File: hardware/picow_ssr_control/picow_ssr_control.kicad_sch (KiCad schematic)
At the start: 29 parts, among them Q1 IRF4905PBF, Q2 DMG2301L, U1 RaspberryPi-PicoW, U2 ULN2803A

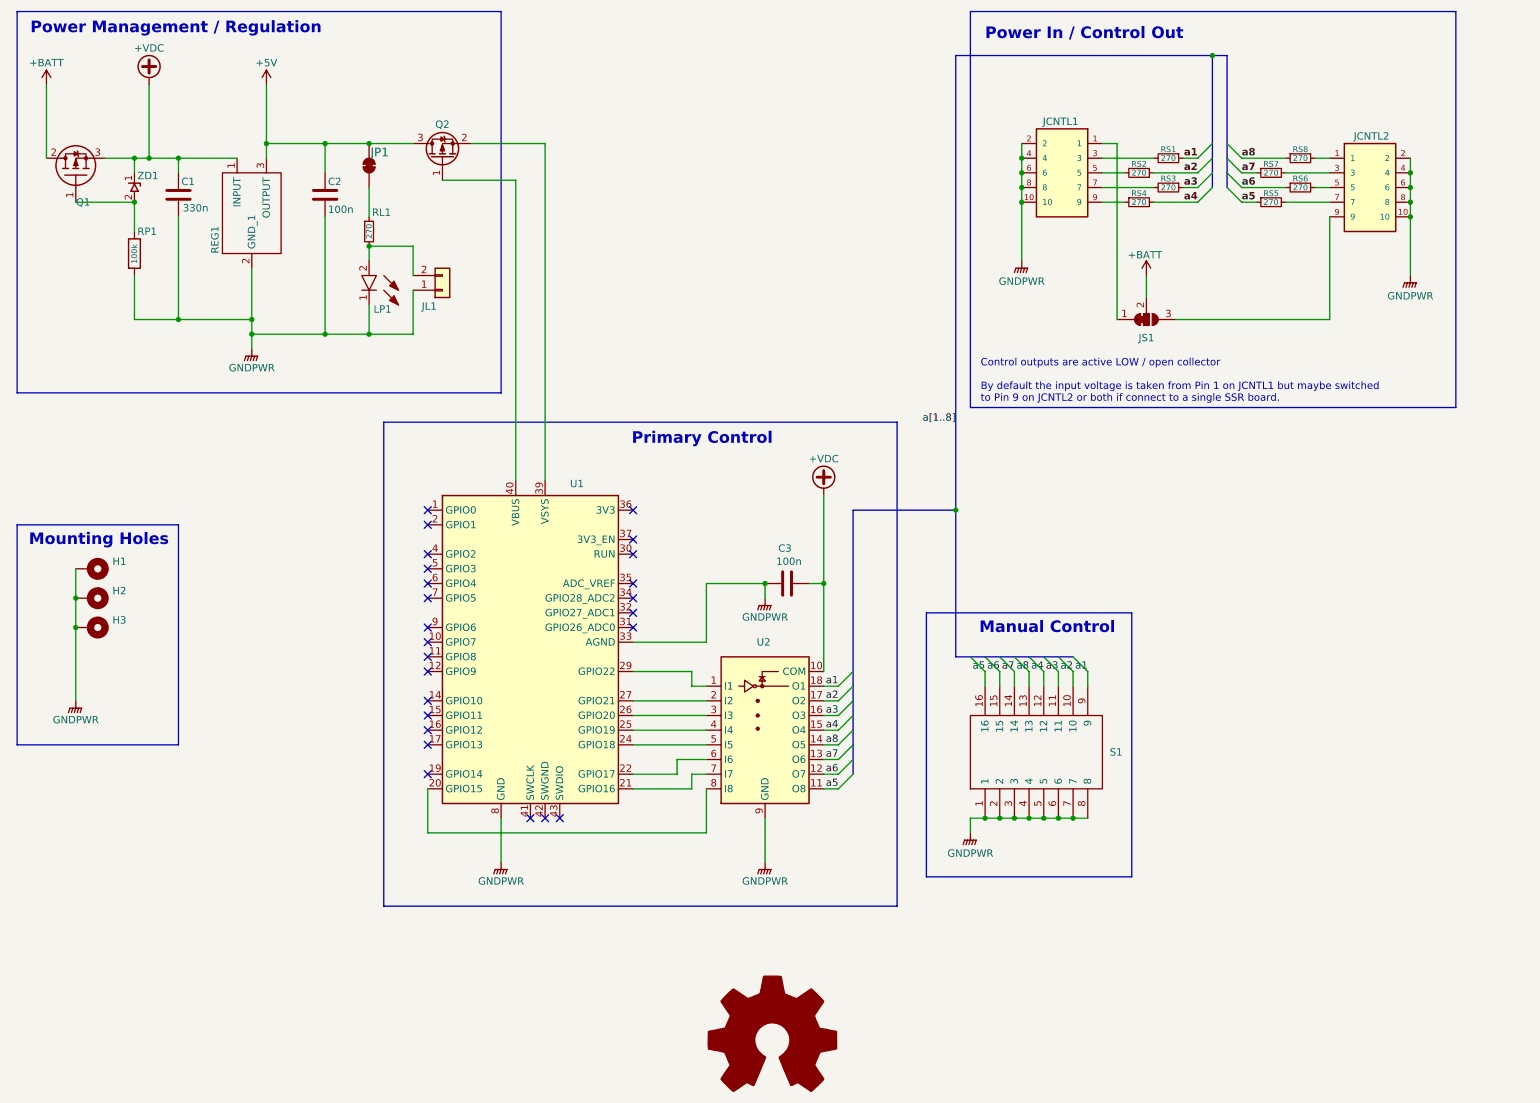
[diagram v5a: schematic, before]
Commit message: Replaced un-obtainable ULN2803 with SMD FETs and updated control connectors
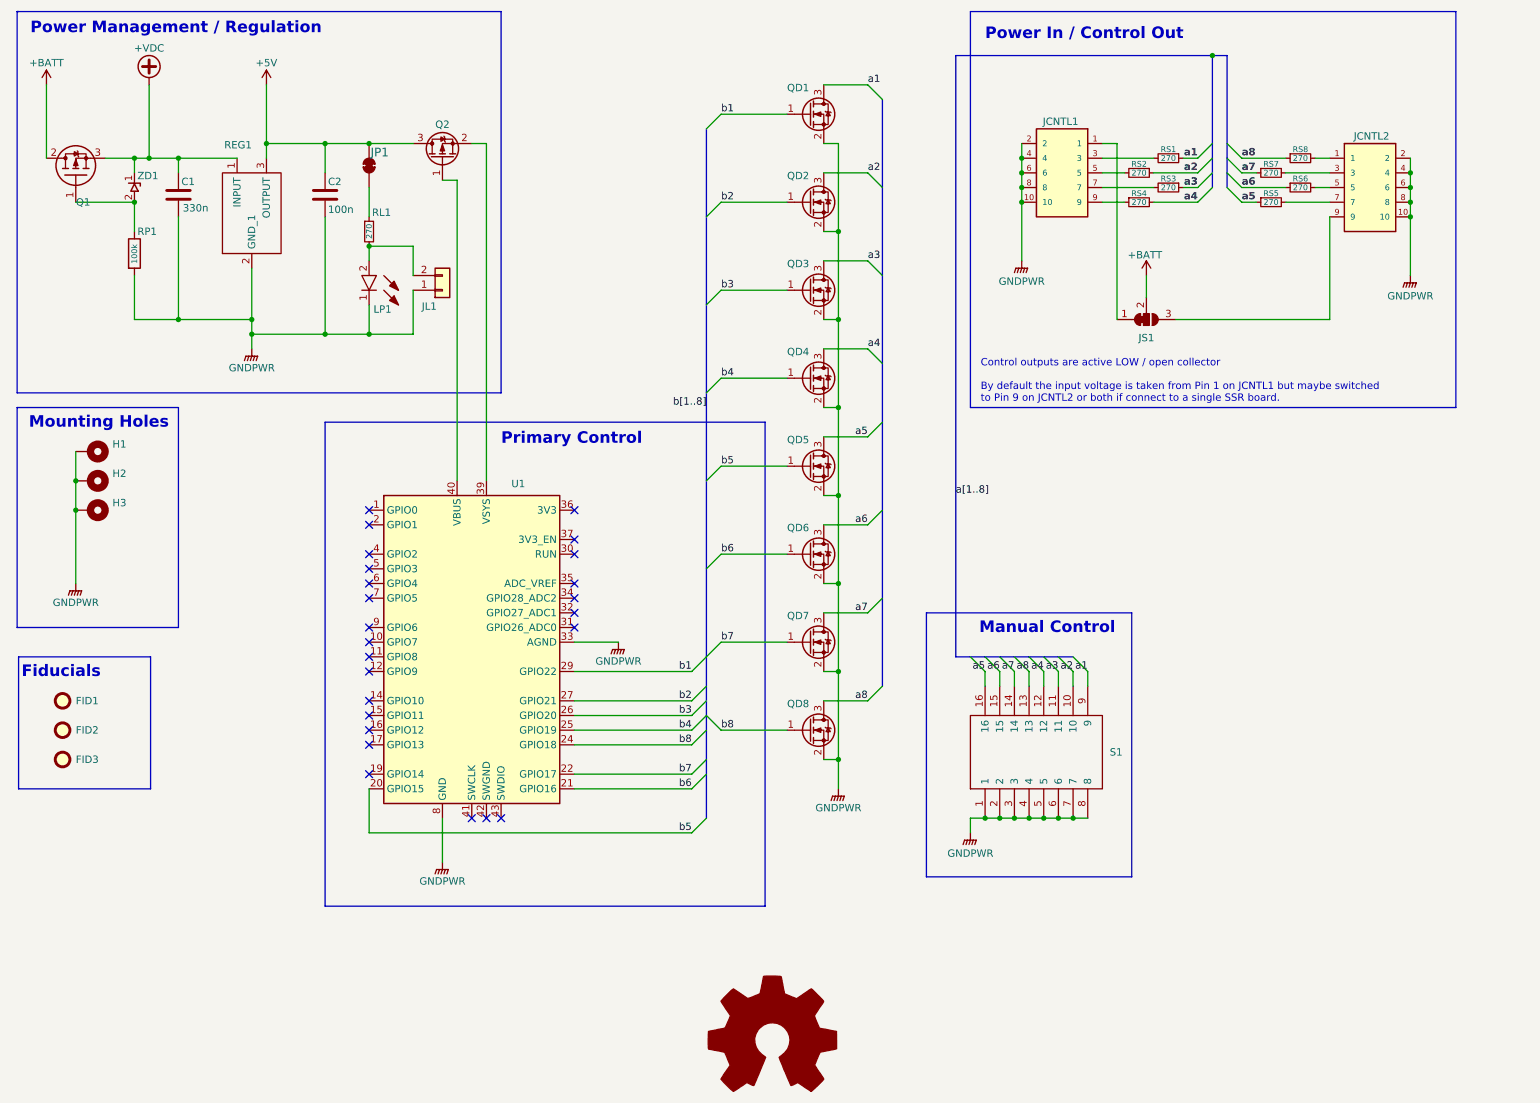
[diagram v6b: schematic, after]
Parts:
- removed C3: 100n, Capacitor_SMD:C_0805_2012Metric, symbol Device:C
- removed U2: ULN2803A, Package_DIP:DIP-18_W7.62mm, symbol Transistor_Array:ULN2805A
- added FID1, FID2, FID3: Fiducial, Fiducial:Fiducial_0.5mm_Mask1mm, symbol Mechanical:Fiducial
- added QD1, QD2, QD3, QD4, QD5, QD6, QD7, QD8: 2N7002K, Package_TO_SOT_SMD:SOT-23, symbol Transistor_FET:2N7002K
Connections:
- net GNDPWR: now also QD1.2 (S), QD2.2 (S), QD3.2 (S), QD4.2 (S), QD5.2 (S), QD6.2 (S), QD7.2 (S), QD8.2 (S)
- net a1: now also QD1.3 (D)
- net a2: now also QD2.3 (D)
- net a3: now also QD3.3 (D)
- net a4: now also QD4.3 (D)
- net a5: now also QD5.3 (D)
- net a6: now also QD6.3 (D)
- net a7: now also QD7.3 (D)
- net a8: now also QD8.3 (D)
- net b5: now reaches U1.20 (GPIO15)
- net b5: now also QD5.1 (G)
- net b6: now reaches U1.21 (GPIO16)
- net b6: now also QD6.1 (G)
- net b7: now reaches U1.22 (GPIO17)
- net b7: now also QD7.1 (G)
- net b8: now reaches U1.24 (GPIO18)
- net b8: now also QD8.1 (G)
- net b4: now reaches U1.25 (GPIO19)
- net b4: now also QD4.1 (G)
- net b3: now reaches U1.26 (GPIO20)
- net b3: now also QD3.1 (G)
- net b2: now reaches U1.27 (GPIO21)
- net b2: now also QD2.1 (G)
- net b1: now reaches U1.29 (GPIO22)
- net b1: now also QD1.1 (G)
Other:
- note added: "Fiducials"
- moved on the sheet: H1, H2, H3, U1
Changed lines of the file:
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@@
   (title_block
     (title "Picow SSR Control")
-    (date "2022-12-07")
+    (date "2022-12-22")
     (rev "0.0.7")
     (comment 2 "http://creativecommons.org/licenses/by-sa/4.0/")

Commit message: Misc minor updates after tag
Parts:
- added JS2: Conn_01x02, Connector_PinHeader_1.00mm:PinHeader_1x02_P1.00mm_Vertical, symbol Connector_Generic:Conn_01x02
- JL1: now in the parts list
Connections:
- net +BATT: now also JS2.1 (Pin_1)
- net GNDPWR: now also JS2.2 (Pin_2)
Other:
- note added: "Control outputs are active LOW / open drain (collector) By default the input voltage is taken from Pin 1 on JCNTL1 but maybe switched to Pin 9 on JCNTL2 or both if connect to a single SSR board. Optional both can be disconnected and power supplied via JS2 but care must be taken to insure there is a common ground between this control board, power input, and the SSR board."
- note added: "PicoW Control / Drivers"
- note removed: "Control outputs are active LOW / open collector By default the input voltage is taken from Pin 1 on JCNTL1 but maybe switched to Pin 9 on JCNTL2 or both if connect to a single SSR board."
- note removed: "Primary Control"
- moved on the sheet: QD1, QD2, QD3, QD4, QD5, QD6, QD7, QD8, U1

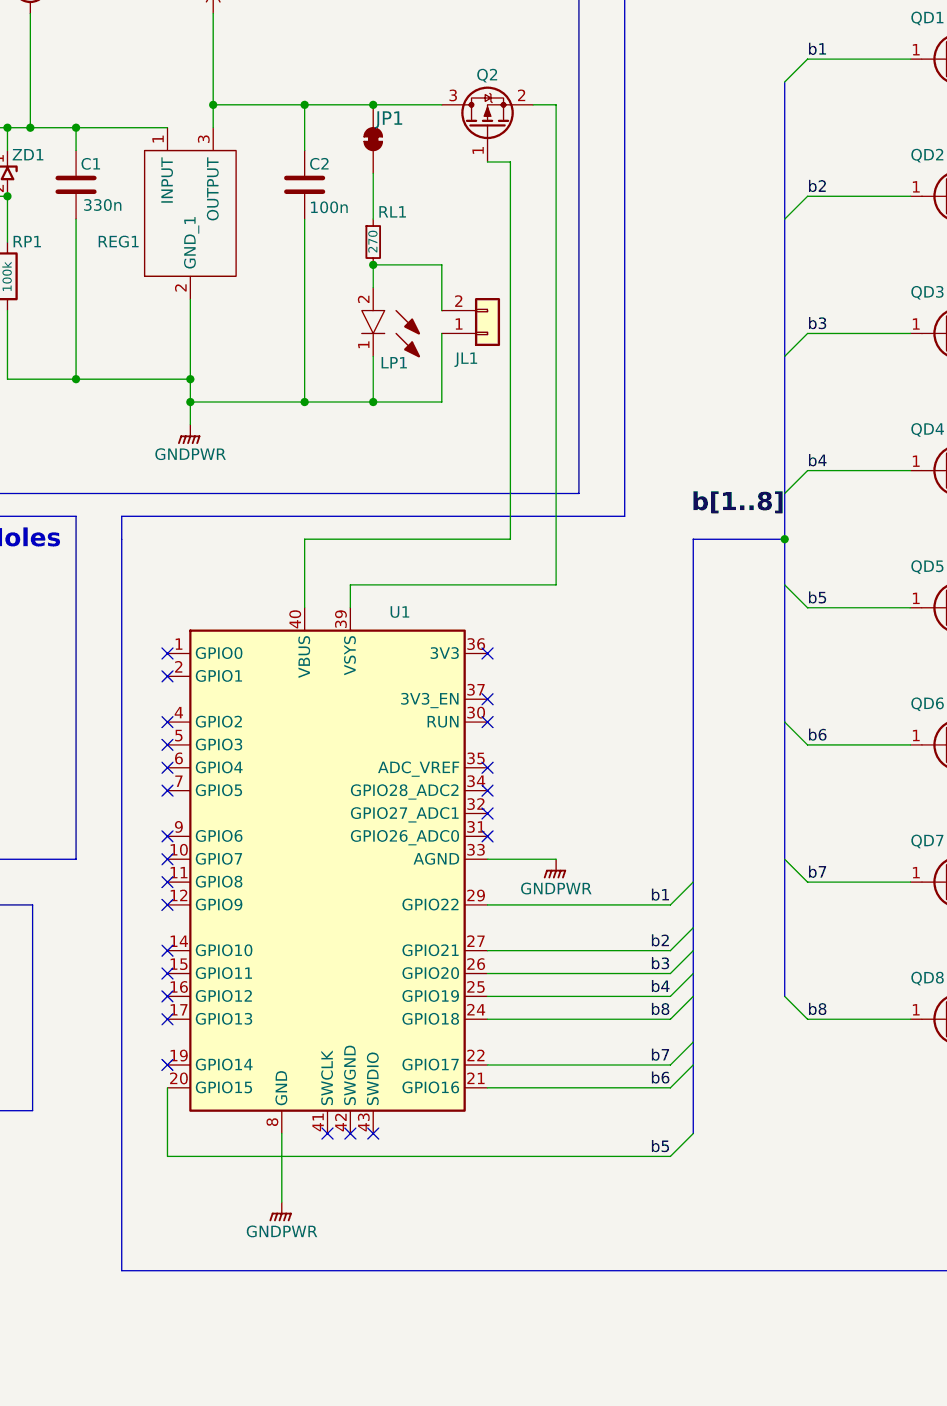
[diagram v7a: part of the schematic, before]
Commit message: Vertical Pico, Moved connectors, and draft production files
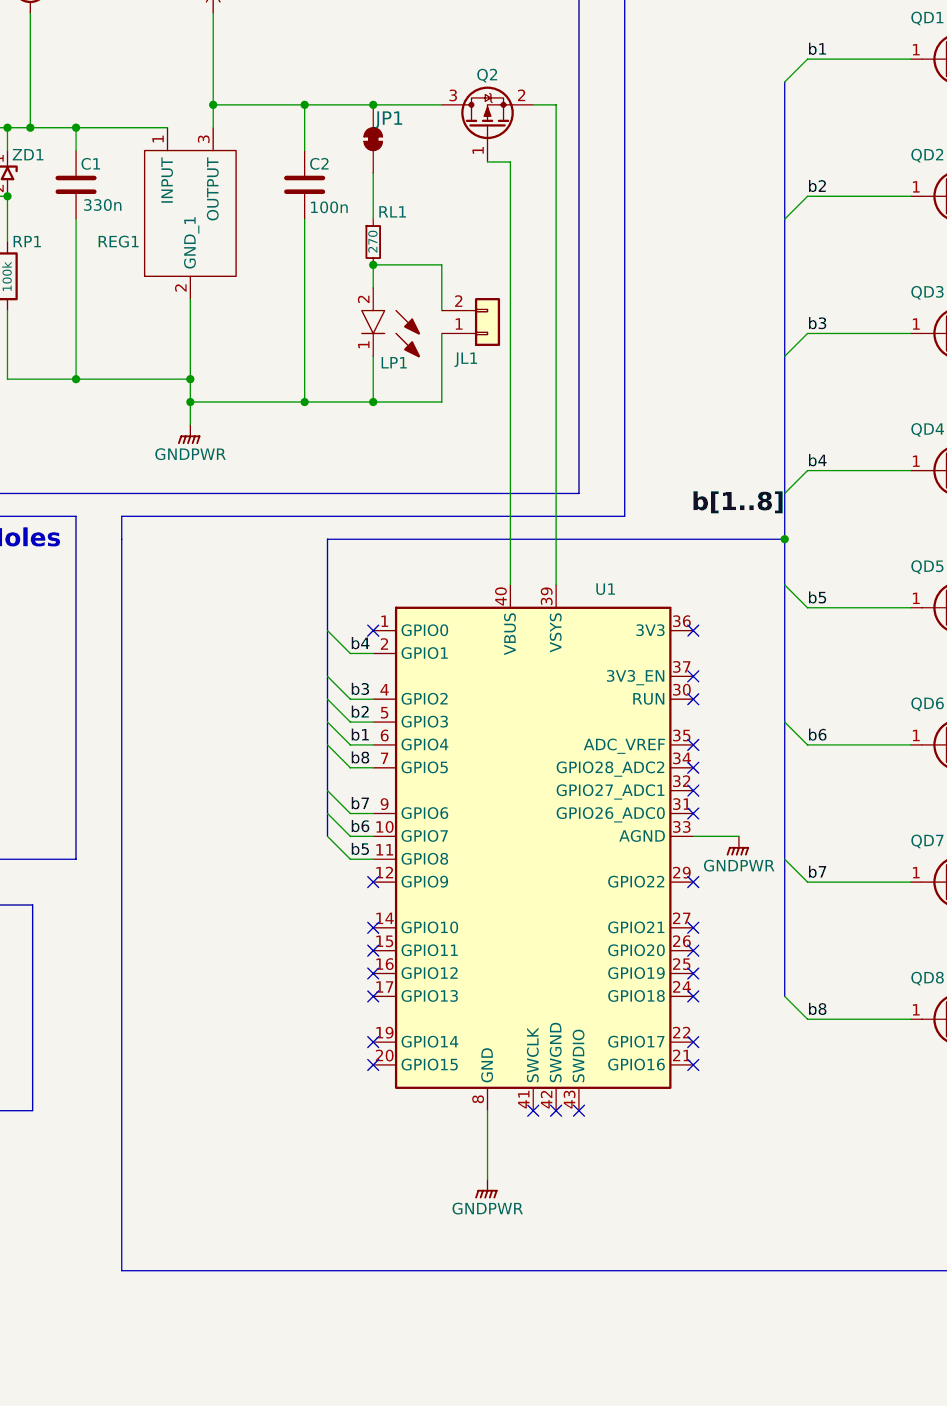
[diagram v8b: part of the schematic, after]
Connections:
- net b1: now also U1.6 (GPIO4); no longer U1.29 (GPIO22)
- net b2: now also U1.5 (GPIO3); no longer U1.27 (GPIO21)
- net b3: now also U1.4 (GPIO2); no longer U1.26 (GPIO20)
- net b4: now also U1.2 (GPIO1); no longer U1.25 (GPIO19)
- net b5: now also U1.11 (GPIO8); no longer U1.20 (GPIO15)
- net b6: now also U1.10 (GPIO7); no longer U1.21 (GPIO16)
- net b7: now also U1.9 (GPIO6); no longer U1.22 (GPIO17)
- net b8: now also U1.7 (GPIO5); no longer U1.24 (GPIO18)
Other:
- moved on the sheet: U1
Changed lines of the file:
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@@
   (title_block
     (title "Picow SSR Control")
-    (date "2022-12-22")
-    (rev "0.0.7")
+    (date "2023-01-02")
+    (rev "0.0.8")
     (comment 2 "http://creativecommons.org/licenses/by-sa/4.0/")
     (comment 3 "License: CC By SA 4.0")
